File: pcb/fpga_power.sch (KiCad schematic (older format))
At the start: 77 parts

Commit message: schematic completed. Time for review
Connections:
- net VCCAUX is gone; now on net +1V8: C?.1, C?.1, C?.1, C?.1, C?.1, C?.1, C?.1, C?.1, U?.H12 (VCCAUX), U?.K12 (VCCAUX), U?.M12 (VCCAUX), U?.P12 (VCCAUX), U?.R11 (VCCAUX)
- net VCCBRAM is gone; now on net +1V0: C?.1, C?.1, U?.J11 (VCCBRAM), U?.L11 (VCCBRAM), U?.N11 (VCCBRAM)
- net VCCINT is gone; now on net +1V0: C?.1, C?.1, C?.1, C?.1, C?.1, C?.1, C?.1, C?.1, C?.1, C?.1, C?.1, U?.H10 (VCCINT), U?.H8 (VCCINT), U?.J7 (VCCINT), U?.J9 (VCCINT), U?.K8 (VCCINT), U?.L7 (VCCINT), U?.M8 (VCCINT), U?.N7 (VCCINT), U?.P10 (VCCINT), U?.P8 (VCCINT), U?.R7 (VCCINT), U?.R9 (VCCINT), U?.T10 (VCCINT), U?.T8 (VCCINT)
- net VCCO_13 is gone; now on net +3V3: C?.1, C?.1, C?.1, C?.1, C?.1, C?.1, C?.1, U?.AA17 (VCCO_13), U?.AB14 (VCCO_13), U?.V16 (VCCO_13), U?.W13 (VCCO_13), U?.Y10 (VCCO_13)
- net VCCO_14 is gone; now on net +3V3: C?.1, C?.1, C?.1, C?.1, C?.1, C?.1, C?.1, U?.M14 (VCCO_14), U?.P18 (VCCO_14), U?.R15 (VCCO_14), U?.T22 (VCCO_14), U?.U19 (VCCO_14), U?.Y20 (VCCO_14)
- net VCCO_15 is gone; now on net +3V3: C?.1, C?.1, C?.1, C?.1, C?.1, C?.1, C?.1, U?.G19 (VCCO_15), U?.H16 (VCCO_15), U?.J13 (VCCO_15), U?.K20 (VCCO_15), U?.L17 (VCCO_15), U?.N21 (VCCO_15)
- net VCCO_16 is gone; now on net +3V3: C?.1, C?.1, C?.1, C?.1, C?.1, C?.1, C?.1, U?.A17 (VCCO_16), U?.B14 (VCCO_16), U?.C21 (VCCO_16), U?.D18 (VCCO_16), U?.E15 (VCCO_16), U?.F22 (VCCO_16)
- net VCCO_34 is gone; now on net +3V3: C?.1, C?.1, C?.1, C?.1, C?.1, C?.1, C?.1, U?.AB4 (VCCO_34), U?.R5 (VCCO_34), U?.T2 (VCCO_34), U?.V6 (VCCO_34), U?.W3 (VCCO_34)
- net +1V2: now reaches FB?.1
- net +1V0: now reaches FB?.1
- net +1V8: now reaches FB?.1
- net VCCO_0 renamed +3V3
- net VCCO_35 renamed +1V5
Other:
- note added: "DDR-3 on bank 35, 1.5V IO. All others 3.3V"
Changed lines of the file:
@@
 LIBS:valves
 LIBS:wbraun_ic_lib
-LIBS:xilinx-artix7
-LIBS:FMC_connector-cache
+LIBS:pgmfoot
 LIBS:artix7_pcie_pcb-cache
 EELAYER 25 0
@@
 $Descr A4 11693 8268
 encoding utf-8
-Sheet 4 10
+Sheet 4 12
 Title ""
 Date ""
@@
 Connection ~ 10350 1350
 Wire Wire Line
-	8850 1050 8850 950
+	8850 900  8850 1050
 Wire Wire Line
 	8850 950  8650 950
@@
 Connection ~ 10350 2250
 Wire Wire Line
-	8850 1950 8850 1850
+	8850 1800 8850 1950
 Wire Wire Line
 	8850 1850 8650 1850
@@
 Connection ~ 10350 3150
 Wire Wire Line
-	8850 2850 8850 2750
+	8850 2650 8850 2850
 Wire Wire Line
 	8850 2750 8650 2750
@@
 Connection ~ 7700 1350
 Wire Wire Line
-	6200 1050 6200 950
+	6200 900  6200 1050
 Wire Wire Line
 	6200 950  6000 950
@@
 Connection ~ 7700 2250
 Wire Wire Line
-	6200 1950 6200 1850
+	6200 1800 6200 1950
 Wire Wire Line
 	6200 1850 6000 1850
@@
 Connection ~ 7700 3150
 Wire Wire Line
-	6200 2850 6200 2750
+	6200 2700 6200 2850
 Wire Wire Line
 	6200 2750 6000 2750
@@
 	10650 4050 10650 4150
 Wire Wire Line
-	10650 3750 10650 3650
+	10650 3600 10650 3750
 Wire Wire Line
 	10650 3650 10450 3650
@@
 $EndComp
 Wire Wire Line
-	6800 3700 6800 3600
+	6800 3550 6800 3700
 Wire Wire Line
 	6800 3600 6600 3600
@@
 Connection ~ 8300 4800
 Wire Wire Line
-	6200 4500 6200 4400
+	6200 4300 6200 4500
 Wire Wire Line
 	6200 4400 6000 4400
@@
 	10350 4800 10350 4900
 Wire Wire Line
-	10350 4500 10350 4400
+	10350 4300 10350 4500
 Wire Wire Line
 	10150 4400 10650 4400
@@
 Text Label 1000 4600 2    60   ~ 0
 VCCADC
+Text Notes 1350 6600 0    60   ~ 0
+DDR-3 on bank 35, 1.5V IO. All others 3.3V
+$Comp
+L +1V0 #PWR?
+U 1 1 5660B5F1
+P 6800 3550
+F 0 "#PWR?" H 6800 3400 50  0001 C CNN
+F 1 "+1V0" H 6800 3690 50  0000 C CNN
+F 2 "" H 6800 3550 60  0000 C CNN
+F 3 "" H 6800 3550 60  0000 C CNN
+	1    6800 3550
+	1    0    0    -1
+$EndComp
+$Comp
+L +1V0 #PWR?
+U 1 1 5660B69F
+P 10350 4300
+F 0 "#PWR?" H 10350 4150 50  0001 C CNN
+F 1 "+1V0" H 10350 4440 50  0000 C CNN
+F 2 "" H 10350 4300 60  0000 C CNN
+F 3 "" H 10350 4300 60  0000 C CNN
+	1    10350 4300
+	1    0    0    -1
+$EndComp
+$Comp
+L +1V2 #PWR?
+U 1 1 5660B8CE
+P 5550 5300
+F 0 "#PWR?" H 5550 5150 50  0001 C CNN
+F 1 "+1V2" H 5550 5440 50  0000 C CNN
+F 2 "" H 5550 5300 60  0000 C CNN
+F 3 "" H 5550 5300 60  0000 C CNN
+	1    5550 5300
+	1    0    0    -1
+$EndComp
+$Comp
+L +1V0 #PWR?
+U 1 1 5660B97C
+P 7300 5300
+F 0 "#PWR?" H 7300 5150 50  0001 C CNN
+F 1 "+1V0" H 7300 5440 50  0000 C CNN
+F 2 "" H 7300 5300 60  0000 C CNN
+F 3 "" H 7300 5300 60  0000 C CNN
+	1    7300 5300
+	1    0    0    -1
+$EndComp
+$Comp
+L +1V8 #PWR?
+U 1 1 5660BA2A
+P 5250 6000
+F 0 "#PWR?" H 5250 5850 50  0001 C CNN
+F 1 "+1V8" H 5250 6140 50  0000 C CNN
+F 2 "" H 5250 6000 60  0000 C CNN
+F 3 "" H 5250 6000 60  0000 C CNN
+	1    5250 6000
+	1    0    0    -1
+$EndComp
+$Comp
+L +1V8 #PWR?
+U 1 1 5660BAD8
+P 6200 4300
+F 0 "#PWR?" H 6200 4150 50  0001 C CNN
+F 1 "+1V8" H 6200 4440 50  0000 C CNN
+F 2 "" H 6200 4300 60  0000 C CNN
+F 3 "" H 6200 4300 60  0000 C CNN
+	1    6200 4300
+	1    0    0    -1
+$EndComp
+$Comp
+L +1V5 #PWR?
+U 1 1 5660BB86
+P 8850 2650
+F 0 "#PWR?" H 8850 2500 50  0001 C CNN
+F 1 "+1V5" H 8850 2790 50  0000 C CNN
+F 2 "" H 8850 2650 60  0000 C CNN
+F 3 "" H 8850 2650 60  0000 C CNN
+	1    8850 2650
+	1    0    0    -1
+$EndComp
+$Comp
+L +3V3 #PWR?
+U 1 1 5660BC34
+P 8850 1800
+F 0 "#PWR?" H 8850 1650 50  0001 C CNN
+F 1 "+3V3" H 8850 1940 50  0000 C CNN
+F 2 "" H 8850 1800 60  0000 C CNN
+F 3 "" H 8850 1800 60  0000 C CNN
+	1    8850 1800
+	1    0    0    -1
+$EndComp
+$Comp
+L +3V3 #PWR?
+U 1 1 5660BCE2
+P 8850 900
+F 0 "#PWR?" H 8850 750 50  0001 C CNN
+F 1 "+3V3" H 8850 1040 50  0000 C CNN
+F 2 "" H 8850 900 60  0000 C CNN
+F 3 "" H 8850 900 60  0000 C CNN
+	1    8850 900
+	1    0    0    -1
+$EndComp
+$Comp
+L +3V3 #PWR?
+U 1 1 5660BD90
+P 6200 900
+F 0 "#PWR?" H 6200 750 50  0001 C CNN
+F 1 "+3V3" H 6200 1040 50  0000 C CNN
+F 2 "" H 6200 900 60  0000 C CNN
+F 3 "" H 6200 900 60  0000 C CNN
+	1    6200 900
+	1    0    0    -1
+$EndComp
+$Comp
+L +3V3 #PWR?
+U 1 1 5660BE3E
+P 6200 1800
+F 0 "#PWR?" H 6200 1650 50  0001 C CNN
+F 1 "+3V3" H 6200 1940 50  0000 C CNN
+F 2 "" H 6200 1800 60  0000 C CNN
+F 3 "" H 6200 1800 60  0000 C CNN
+	1    6200 1800
+	1    0    0    -1
+$EndComp
+$Comp
+L +3V3 #PWR?
+U 1 1 5660BEEC
+P 6200 2700
+F 0 "#PWR?" H 6200 2550 50  0001 C CNN
+F 1 "+3V3" H 6200 2840 50  0000 C CNN
+F 2 "" H 6200 2700 60  0000 C CNN
+F 3 "" H 6200 2700 60  0000 C CNN
+	1    6200 2700
+	1    0    0    -1
+$EndComp
+$Comp
+L +3V3 #PWR?
+U 1 1 5660C1B5
+P 10650 3600
+F 0 "#PWR?" H 10650 3450 50  0001 C CNN
+F 1 "+3V3" H 10650 3740 50  0000 C CNN
+F 2 "" H 10650 3600 60  0000 C CNN
+F 3 "" H 10650 3600 60  0000 C CNN
+	1    10650 3600
+	1    0    0    -1
+$EndComp
+Connection ~ 6200 950
+Connection ~ 8850 950
+Connection ~ 8850 1850
+Connection ~ 6200 1850
+Connection ~ 6200 2750
+Connection ~ 8850 2750
+Connection ~ 6800 3600
+Connection ~ 6200 4400
+Wire Wire Line
+	7300 5300 7300 5400
+Wire Wire Line
+	7300 5400 7350 5400
+Wire Wire Line
+	5550 5300 5550 5400
+Wire Wire Line
+	5550 5400 5600 5400
+Wire Wire Line
+	5250 6000 5250 6100
+Wire Wire Line
+	5250 6100 5300 6100
+Connection ~ 10650 3650
+Text GLabel 6350 5000 2    60   Input ~ 0
+MGTAVTT
 $EndSCHEMATC

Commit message: Added part numbers and updated schematic
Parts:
- gave numbers to parts that had none: 77

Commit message: mostly done with component placement
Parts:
- added C402, C407: 4.7uF, wbraun_smd:C_0402, symbol C
- added C436, C441: 0.47uF, wbraun_smd:C_0402, symbol C
- C401: renamed from C416; footprint (none) -> wbraun_smd:TantalC_SizeD_EIA-7343
- C403: renamed from C401; footprint (none) -> wbraun_smd:C_0402
- C404: renamed from C402; footprint (none) -> wbraun_smd:C_0805
- C405: renamed from C403; footprint (none) -> wbraun_smd:C_0805
- C406: renamed from C404; footprint (none) -> wbraun_smd:C_0805
- C408: renamed from C405; footprint (none) -> wbraun_smd:C_0805
- C409: renamed from C406; footprint (none) -> wbraun_smd:C_0402
- C410: renamed from C407; footprint (none) -> wbraun_smd:C_0402
- C411: renamed from C408; footprint (none) -> wbraun_smd:C_0402
- C412: renamed from C409; footprint (none) -> wbraun_smd:C_0402
- C413: renamed from C422; footprint (none) -> wbraun_smd:C_0402
- C414: renamed from C410; footprint (none) -> wbraun_smd:C_0402
- C415: renamed from C411; footprint (none) -> wbraun_smd:C_0402
- C416: renamed from C412; footprint (none) -> wbraun_smd:C_0402
- C417: renamed from C413; footprint (none) -> wbraun_smd:C_0402
- C418: renamed from C414; footprint (none) -> wbraun_smd:C_0402
- C419: renamed from C415; footprint (none) -> wbraun_smd:C_0402
- C420: renamed from C427; footprint (none) -> wbraun_smd:C_0402
- C421: renamed from C417; footprint (none) -> wbraun_smd:C_0402
- C422: renamed from C418; footprint (none) -> wbraun_smd:C_0402
- C423: renamed from C419; footprint (none) -> wbraun_smd:C_0402
- C424: renamed from C420; footprint (none) -> wbraun_smd:C_0402
- C425: renamed from C421; footprint (none) -> wbraun_smd:C_0402
- C426: renamed from C432; footprint (none) -> wbraun_smd:C_0402
- C427: renamed from C423; footprint (none) -> wbraun_smd:C_0402
- C428: renamed from C424; footprint (none) -> wbraun_smd:C_0402
- C429: renamed from C425; footprint (none) -> wbraun_smd:C_0402
- C430: renamed from C426; footprint (none) -> wbraun_smd:C_0402
- C431: renamed from C437; footprint (none) -> wbraun_smd:C_0402
- C432: renamed from C428; footprint (none) -> wbraun_smd:C_0402
- C433: renamed from C429; footprint (none) -> wbraun_smd:C_0402
- C434: renamed from C430; footprint (none) -> wbraun_smd:C_0402
- C435: renamed from C431; footprint (none) -> wbraun_smd:C_0402
- C437: renamed from C433; footprint (none) -> wbraun_smd:C_0402
- C438: renamed from C434; footprint (none) -> wbraun_smd:C_0402
- C439: renamed from C435; footprint (none) -> wbraun_smd:C_0402
- C440: renamed from C436; footprint (none) -> wbraun_smd:C_0402
- C442: renamed from C438; footprint (none) -> wbraun_smd:C_0402
- C443: renamed from C439; footprint (none) -> wbraun_smd:C_0402
- C444: renamed from C440; footprint (none) -> wbraun_smd:C_0402
- C445: renamed from C441; footprint (none) -> wbraun_smd:C_0402
- C446: renamed from C442; footprint (none) -> wbraun_smd:C_0402
- C447: renamed from C443; footprint (none) -> wbraun_smd:C_0402
- C448: renamed from C444; footprint (none) -> wbraun_smd:C_0402
- C449: renamed from C445; footprint (none) -> wbraun_smd:C_0402
- C450: renamed from C446; footprint (none) -> wbraun_smd:C_0805
- C451: renamed from C447; footprint (none) -> wbraun_smd:C_0805
- C452: renamed from C448; footprint (none) -> wbraun_smd:C_0805
- C453: renamed from C449; footprint (none) -> wbraun_smd:C_0402
- C454: renamed from C450; footprint (none) -> wbraun_smd:C_0402
- C455: renamed from C451; footprint (none) -> wbraun_smd:C_0402
- C456: renamed from C452; footprint (none) -> wbraun_smd:C_0402
- C457: renamed from C453; footprint (none) -> wbraun_smd:C_0402
- C458: renamed from C454; footprint (none) -> wbraun_smd:C_0402
- C459: renamed from C455; footprint (none) -> wbraun_smd:C_0402
- C460: renamed from C456; footprint (none) -> wbraun_smd:C_0402
- C461: renamed from C457; footprint (none) -> wbraun_smd:C_0402
- C462: renamed from C458; footprint (none) -> wbraun_smd:C_0402
- C463: renamed from C459; footprint (none) -> wbraun_smd:C_0402
- C464: renamed from C460; footprint (none) -> wbraun_smd:C_0402
- C465: renamed from C461; footprint (none) -> wbraun_smd:C_0402
- C466: renamed from C462; footprint (none) -> wbraun_smd:C_0402
- C467: renamed from C463; footprint (none) -> wbraun_smd:C_0402
- C468: renamed from C464; footprint (none) -> wbraun_smd:C_0402
- C469: renamed from C465; footprint (none) -> wbraun_smd:C_0402
- C470: renamed from C466; footprint (none) -> wbraun_smd:C_0402
- C471: renamed from C467; footprint (none) -> wbraun_smd:C_0402
- C472: renamed from C468; footprint (none) -> wbraun_smd:C_0805
- C473: renamed from C469; footprint (none) -> wbraun_smd:C_0402
- C474: renamed from C470; footprint (none) -> wbraun_smd:C_0402
- C475: renamed from C471; footprint (none) -> wbraun_smd:C_0402
- C476: renamed from C472; footprint (none) -> wbraun_smd:C_0805
- C477: renamed from C473; footprint (none) -> wbraun_smd:C_0805
- FB401, FB402, FB403: footprint (none) -> wbraun_smd:L_0603
- U401: footprint (none) -> wbraun_smd:BGA_484_22x22_FULLARRAY_1MM
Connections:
- net +1V0: now also C402.1, C407.1, C436.1, C441.1
- net +1V8: now also C427.1
- net GND: now also C402.2, C407.2, C436.2, C441.2
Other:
- note added: "330uF Cap: T520V337M2R5ATE025 \n2917/D/ 7343 package"
- note added: "47uF Caps: 0805\n4.7uF Caps: 0402\n0.47uF Caps: 0402\nfilter beads: 0603\n"
- note added: "Decoupling good for up to XC7A100T"
- moved on the sheet: C401, C413, C420, C426, C431

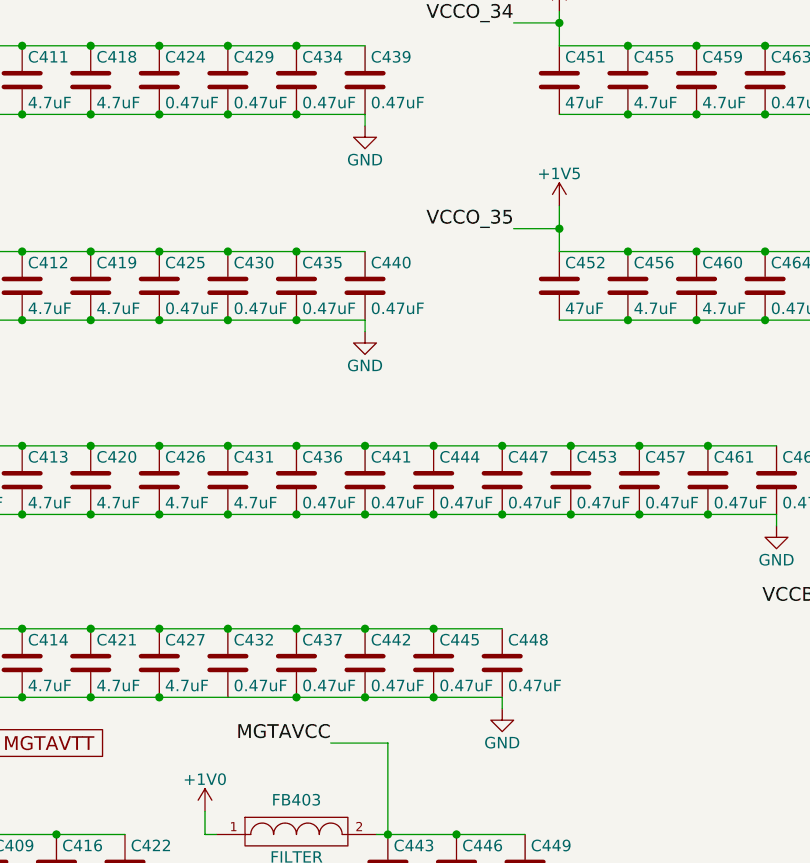
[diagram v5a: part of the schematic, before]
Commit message: Finished most of the routing, removed DDR-3
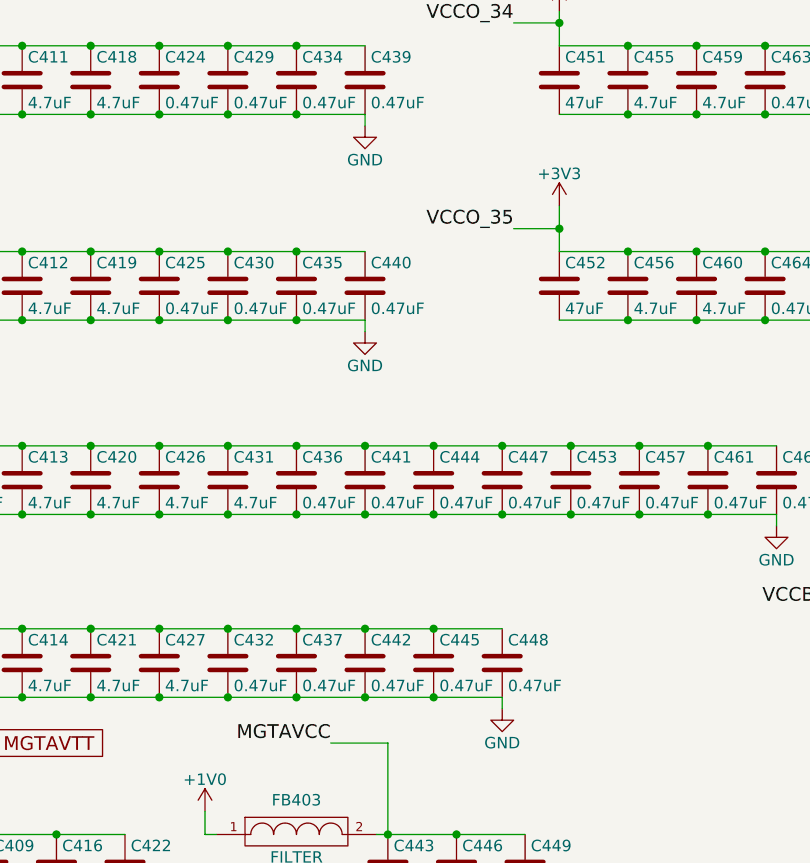
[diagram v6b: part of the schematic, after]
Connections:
- net +1V5 is gone; now on net +3V3: C452.1, C456.1, C460.1, C464.1, C468.1, C471.1, C475.1, U401.C1 (VCCO_35), U401.F2 (VCCO_35), U401.H6 (VCCO_35), U401.J3 (VCCO_35), U401.M4 (VCCO_35), U401.N1 (VCCO_35)
- net GND: now also C432.2
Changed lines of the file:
@@
 $Descr A4 11693 8268
 encoding utf-8
-Sheet 4 13
+Sheet 4 11
 Title ""
 Date ""
@@
 F 3 "" H 6200 4300 60  0000 C CNN
 	1    6200 4300
-	1    0    0    -1
-$EndComp
-$Comp
-L +1V5 #PWR072
-U 1 1 5660BB86
-P 8850 2650
-F 0 "#PWR072" H 8850 2500 50  0001 C CNN
-F 1 "+1V5" H 8850 2790 50  0000 C CNN
-F 2 "" H 8850 2650 60  0000 C CNN
-F 3 "" H 8850 2650 60  0000 C CNN
-	1    8850 2650
 	1    0    0    -1
 $EndComp
@@
 330uF Cap: T520V337M2R5ATE025 \n2917/D/ 7343 package
 Connection ~ 7100 4500
+Connection ~ 7400 4800
+$Comp
+L +3V3 #PWR?
+U 1 1 5677CD69
+P 8850 2650
+F 0 "#PWR?" H 8850 2500 50  0001 C CNN
+F 1 "+3V3" H 8850 2790 50  0000 C CNN
+F 2 "" H 8850 2650 60  0000 C CNN
+F 3 "" H 8850 2650 60  0000 C CNN
+	1    8850 2650
+	1    0    0    -1
+$EndComp
 $EndSCHEMATC

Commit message: power routing finished
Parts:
- C402, C403, C407, C409, C410, C411, C412, C413, C414, C415, C416, C417, C418, C419, C420, C421, C422, C423, C424, C425, C426, C427, C428, C429, C430, C431, C432, C433, C434, C435, C436, C437, C438, C439, C440, C441, C442, C443, C444, C445, C446, C447, C448, C449, C453, C454, C455, C456, C457, C458, C459, C460, C461, C462, C463, C464, C465, C466, C467, C468, C469, C470, C471, C473, C474, C475: footprint wbraun_smd:C_0402 -> wbraun_smd:0402_in_grid
